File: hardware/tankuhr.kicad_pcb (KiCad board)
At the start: 4 copper layers, 50 x 50 mm, 41 parts, among them J1 Conn_01x04_Pin, J2 Conn_01x04_Pin, J3 Conn_01x04_Pin, J4 Micro_SD_Card_Det1, U1 R-78E5.0-0.5, U2 XIAO-ESP32-C3-SMD, U3 MCP6001R

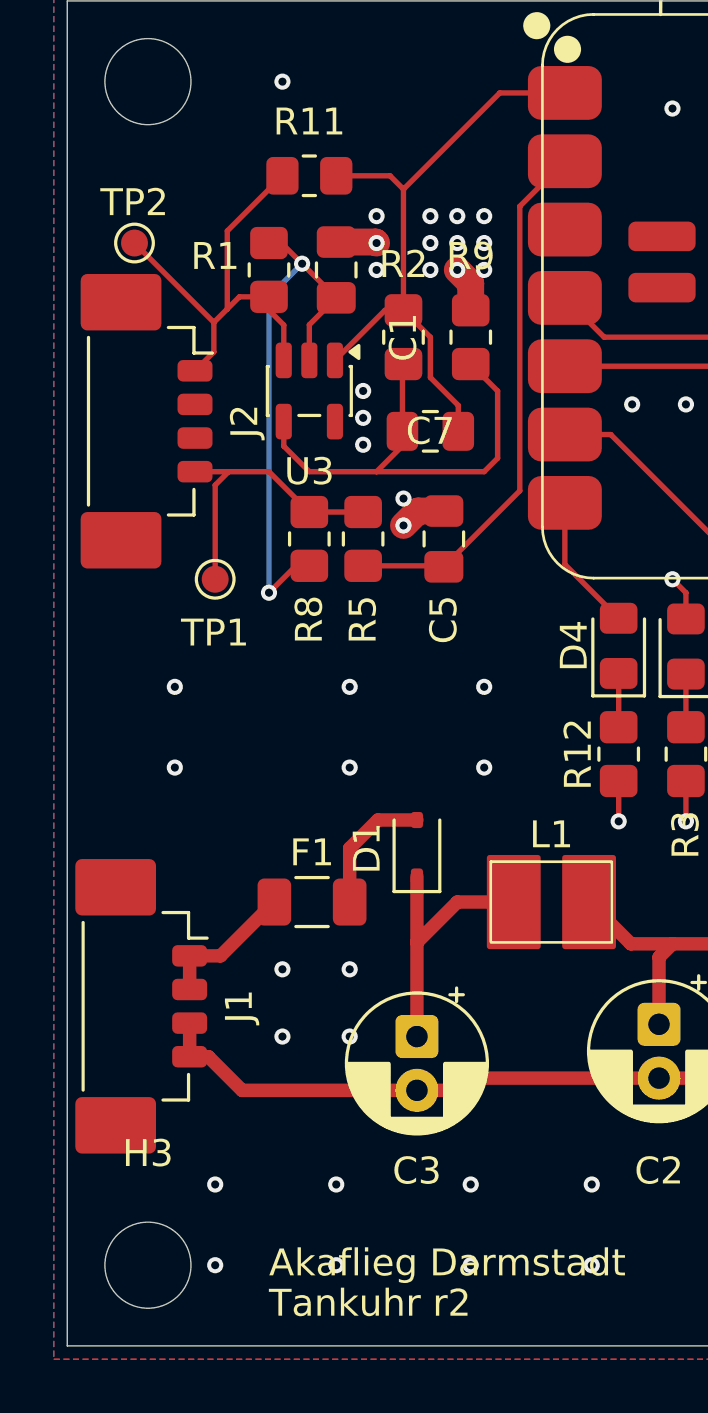
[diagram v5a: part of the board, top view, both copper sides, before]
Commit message: hardware: fix clearing violations
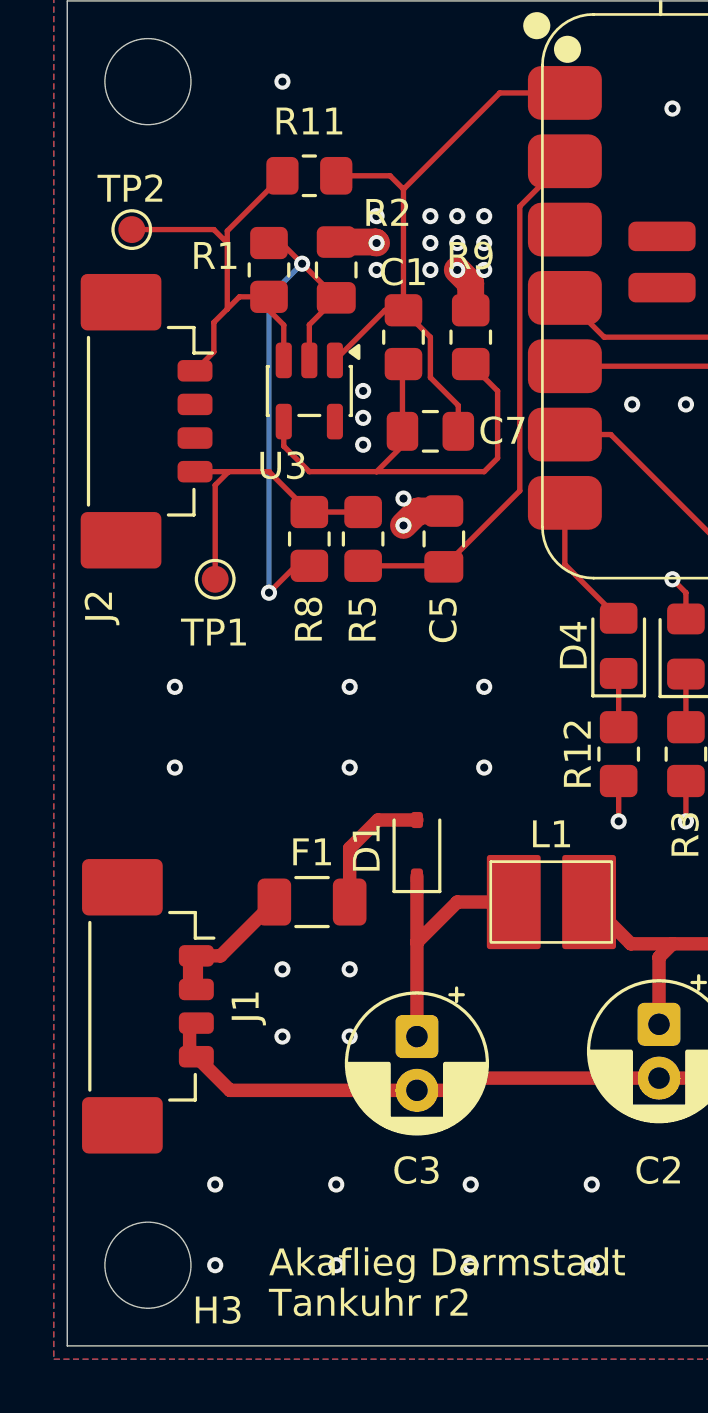
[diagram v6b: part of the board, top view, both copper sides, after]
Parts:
- moved TP2 0.51 mm to (49.9, 56.0)
- moved J1 0.25 mm to (51.0, 84.9)
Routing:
- net Net-(J1-Pin_1): track 5.23 -> 6.48 mm
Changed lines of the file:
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@@
 		(tags "resistor handsolder")
 		(property "Reference" "R2"
-			(at -2.7 0 180)
+			(at -4.6 0.6 180)
 			(layer "F.SilkS")
 			(effects
@@
 		(tags "SOT TO_SOT_SMD")
 		(property "Reference" "U3"
-			(at 3 0 180)
+			(at 2.8 1 180)
 			(layer "F.SilkS")
 			(effects
@@
 		(tags "capacitor handsolder")
 		(property "Reference" "C1"
-			(at -2.5 2.5 90)
+			(at -0.1 2.5 180)
 			(layer "F.SilkS")
 			(effects
@@
 		(tags "capacitor handsolder")
 		(property "Reference" "C7"
-			(at 0 0 0)
+			(at 2.7 0 0)
 			(layer "F.SilkS")
 			(effects
@@
 		(tags "connector Molex PicoBlade vertical")
 		(property "Reference" "J2"
-			(at 0 -3.1 90)
+			(at 6.875 2.3 90)
 			(layer "F.SilkS")
 			(effects
@@
 	(footprint "TestPoint:TestPoint_Pad_D1.0mm"
 		(layer "F.Cu")
-		(at 50 56.5 -90)
+		(at 49.9 56 -90)
 		(descr "SMD pad as test Point, diameter 1.0mm")
 		(tags "test point SMD pad")
@@
 		(tags "mountinghole M3")
 		(property "Reference" "H3"
-			(at 0 -4.15 0)
+			(at 2.6 1.7 0)
 			(layer "F.SilkS")
 			(effects
@@
 	(footprint "Connector_Molex:Molex_PicoBlade_53398-0471_1x04-1MP_P1.25mm_Vertical"
 		(layer "F.Cu")
-		(at 50.8 84.875 -90)
+		(at 51.05 84.875 -90)
 		(descr "Molex PicoBlade series connector, 53398-0471 (http://www.molex.com/pdm_docs/sd/533980271_sd.pdf), generated with kicad-footprint-generator")
 		(tags "connector Molex PicoBlade vertical")
@@
 	(segment
 		(start 53.45 58.95)
-		(end 53.45 56.05)
+		(end 53.45 56.5)
 		(width 0.2)
 		(layer "F.Cu")
@@
 	)
 	(segment
+		(start 53.45 56.5)
+		(end 52.95 56)
+		(width 0.2)
+		(layer "F.Cu")
+		(net 4)
+	)
+	(segment
 		(start 55 58.5)
 		(end 55 59)
@@
 	)
 	(segment
-		(start 50 56.5)
-		(end 52.95 59.45)
+		(start 53.45 58.95)
+		(end 53.9 58.5)
 		(width 0.2)
 		(layer "F.Cu")
@@
 	)
 	(segment
-		(start 53.45 58.95)
-		(end 53.9 58.5)
+		(start 52.95 56)
+		(end 49.9 56)
+		(width 0.2)
+		(layer "F.Cu")
+		(net 4)
+	)
+	(segment
+		(start 53.45 56.5)
+		(end 53.45 56.05)
 		(width 0.2)
 		(layer "F.Cu")
@@
 	)
 	(segment
+		(start 52.3 86.75)
+		(end 53.55 88)
+		(width 0.5)
+		(layer "F.Cu")
+		(net 5)
+	)
+	(segment
 		(start 62 88)
 		(end 62.455112 87.544888)
@@
 	)
 	(segment
+		(start 53.55 88)
+		(end 60.5 88)
+		(width 0.5)
+		(layer "F.Cu")
+		(net 5)
+	)
+	(segment
 		(start 73.5 88)
 		(end 72.25 86.75)
@@
 	)
 	(segment
-		(start 52.75 86.75)
-		(end 52.05 86.75)
-		(width 0.5)
-		(layer "F.Cu")
-		(net 5)
-	)
-	(segment
 		(start 60.5 88)
 		(end 62 88)
@@
 	)
 	(segment
-		(start 54 88)
-		(end 52.75 86.75)
-		(width 0.5)
-		(layer "F.Cu")
-		(net 5)
-	)
-	(segment
-		(start 54 88)
-		(end 60.5 88)
-		(width 0.5)
-		(layer "F.Cu")
-		(net 5)
-	)
-	(segment
 		(start 73.5 89)
 		(end 73.5 88)
@@
 	)
 	(segment
+		(start 52.3 83)
+		(end 52.3 84.25)
+		(width 0.5)
+		(layer "F.Cu")
+		(net 19)
+	)
+	(segment
 		(start 53.2 83)
 		(end 55.2 81)
@@
 	)
 	(segment
-		(start 53.2 83)
+		(start 52.3 83)
 		(end 52.05 83)
-		(width 0.5)
+		(width 0.2)
 		(layer "F.Cu")
 		(net 19)
@@
 		(width 0.5)
 		(layer "F.Cu")
+		(net 19)
+	)
+	(segment
+		(start 52.3 83)
+		(end 53.2 83)
+		(width 0.5)
+		(layer "F.Cu")
